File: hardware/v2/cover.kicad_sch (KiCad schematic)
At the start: 11 parts, among them J401 B2B-XH-A, U401 DRV8876PWPR

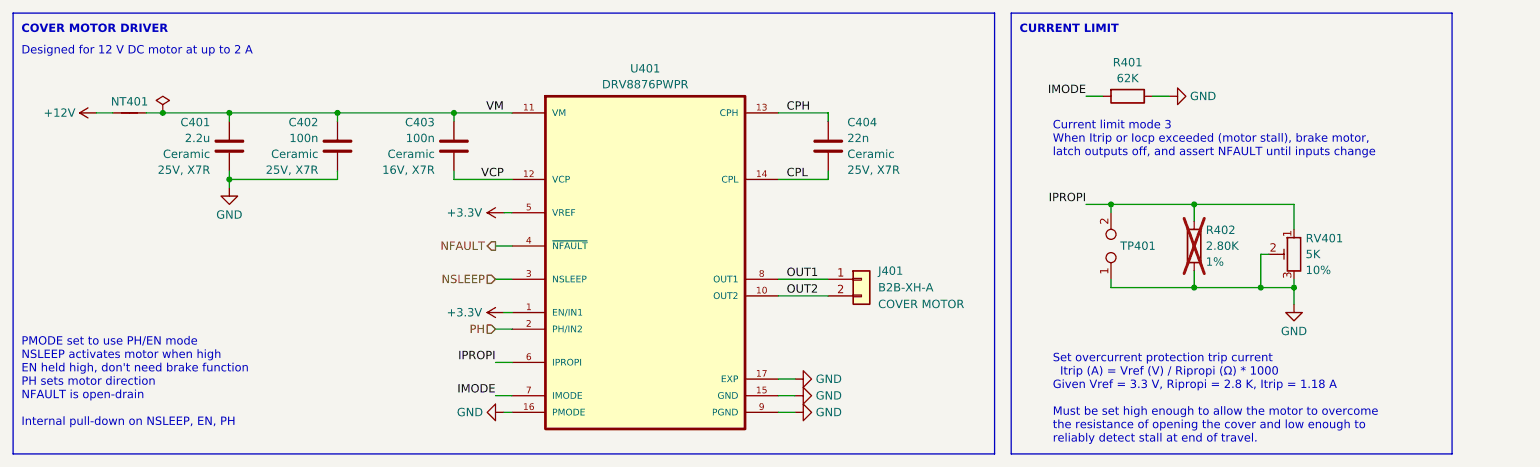
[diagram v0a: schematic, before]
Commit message: Complete draft of the v2 PCB
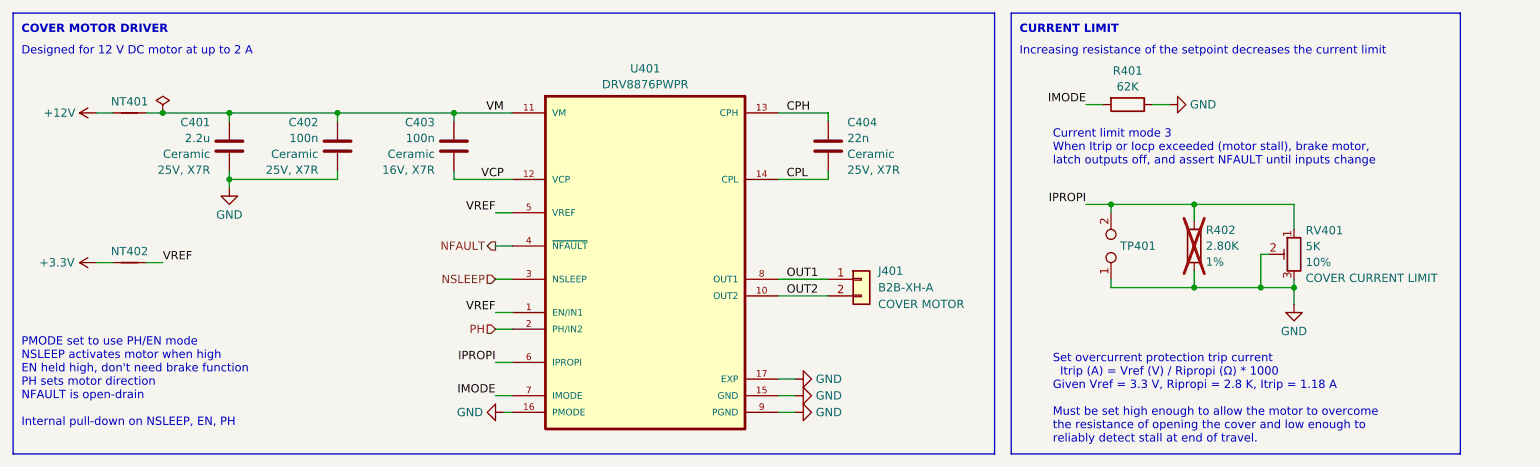
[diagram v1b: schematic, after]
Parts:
- added NT402: NetTie_2, Generic:NetTie-2_SMD_Pad0.2mm, symbol Device:NetTie_2
- RV401: Label (none) -> COVER CURRENT LIMIT
- TP401: footprint TestPoint:TestPoint_2Pads_Pitch5.08mm_Drill1.3mm -> TestPoint:TestPoint_2Pads_Pitch2.54mm_Drill0.8mm
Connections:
- net +3.3V: now also NT402.1; no longer U401.1 (EN/IN1), U401.5 (VREF)
- new net VREF: NT402.2, U401.1 (EN/IN1), U401.5 (VREF)
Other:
- note added: "Increasing resistance of the setpoint decreases the current limit"
- moved on the sheet: R401
